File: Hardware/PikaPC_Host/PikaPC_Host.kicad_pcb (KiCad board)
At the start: 4 copper layers, 101.6 x 101.6 mm, 225 parts, among them J1 DE9_Pins_MountingHoles, J2 DIN41612_03x32_C_Split, J3 Conn_01x03, SW1 SW_Push, U1 PPC403GA, U10 74ALVC164245, U11 74ALVC164245, U12 74ALVC164245, U2 ATF1508AS, U3 MCP120-315GI/TO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

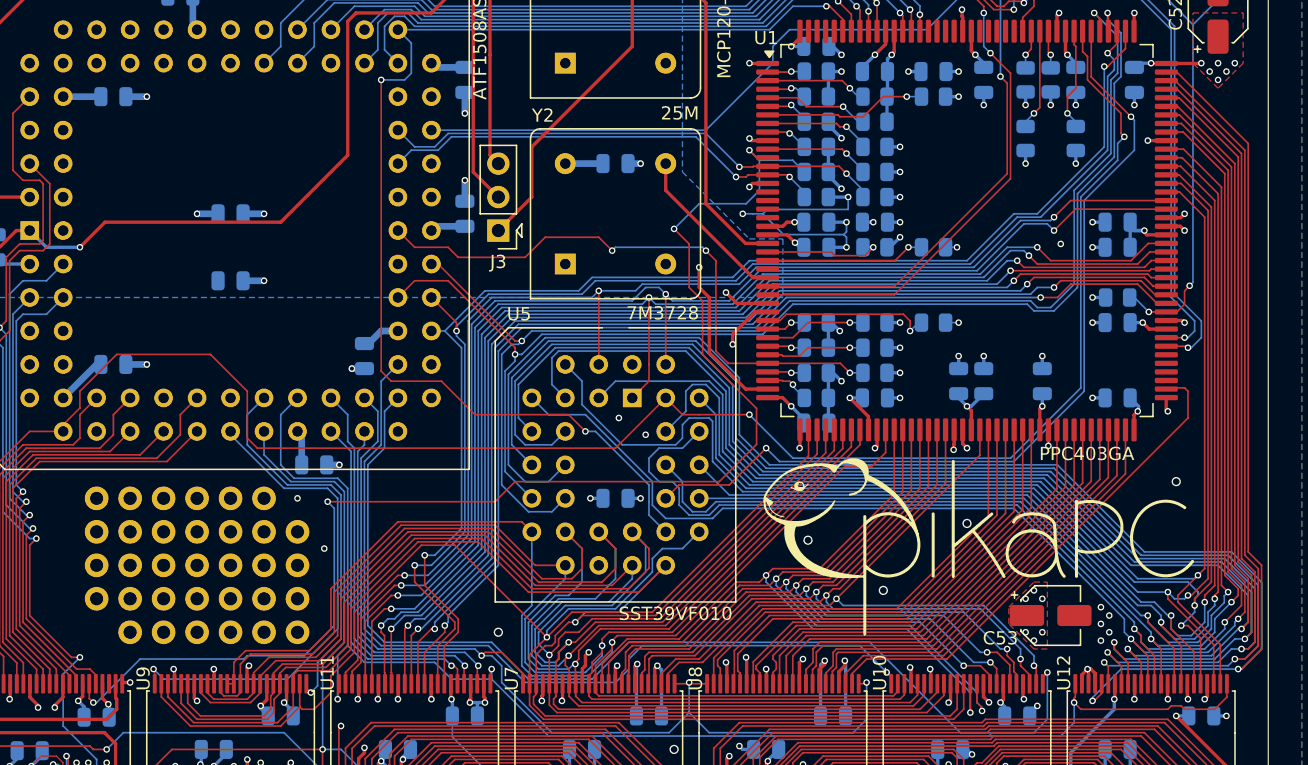
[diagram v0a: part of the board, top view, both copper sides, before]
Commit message: fix low two expansion bus address bits
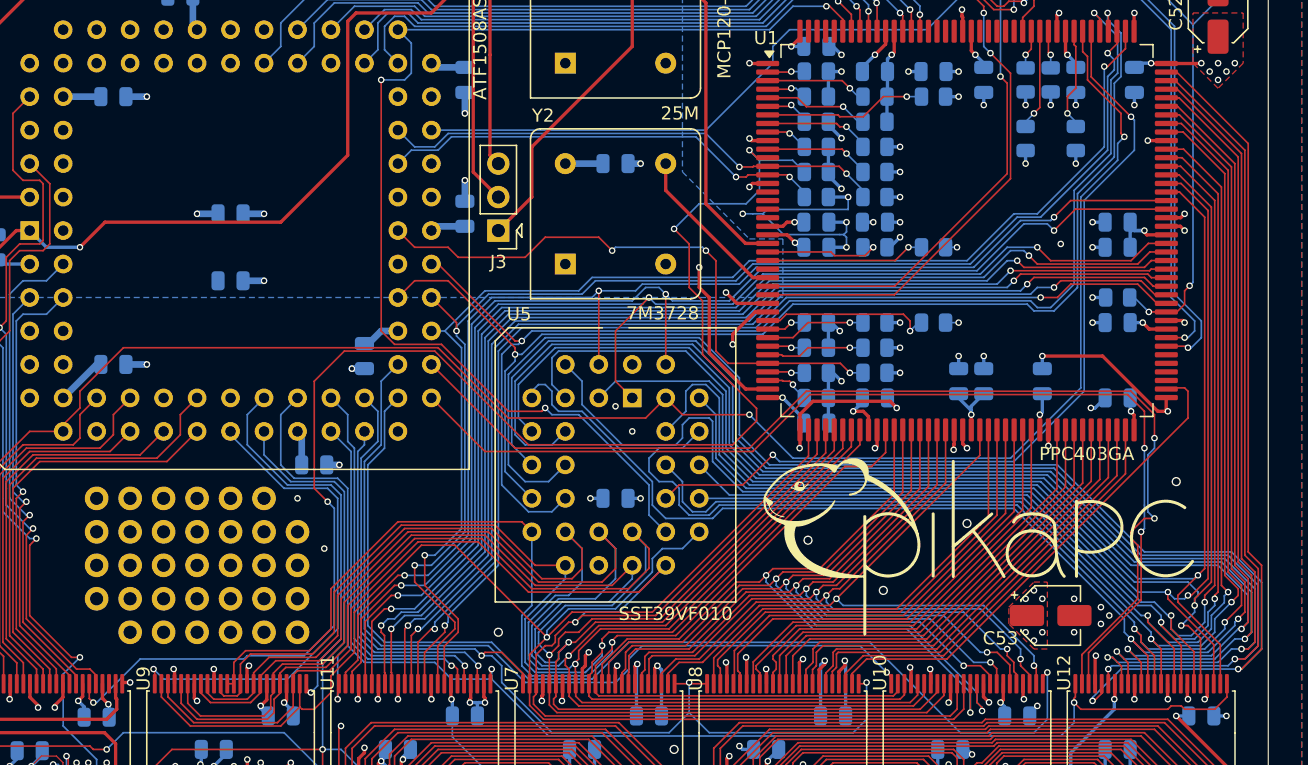
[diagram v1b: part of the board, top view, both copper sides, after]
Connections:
- U12 pad 46: GND -> /Main Bus/XA30
- U12 pad 47: GND -> /Main Bus/XA31
- U2 pad 33: unconnected-(U2A-IO64-Pad33) -> /Main Bus/XA30
- U2 pad 35: unconnected-(U2A-IO59-Pad35) -> /Main Bus/XA31
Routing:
- net /Main Bus/XA31: track 0.00 -> 84.0 mm, vias 0 -> 2
- net /Main Bus/XA30: track 0.00 -> 80.5 mm, vias 0 -> 2
- net GND: track 229.4 -> 248.5 mm
- net /CPU Bus/~{BusError}: track 101.6 -> 113.2 mm
- net /R/~{W}: track 144.1 -> 140.5 mm
- net /Main Bus/A24: track 110.5 -> 112.2 mm
- net /CPU Bus/~{CS0}: track 92.1 -> 90.5 mm
- net /Main Bus/A26: track 134.2 -> 132.6 mm
- net /Main Bus/A13: track 96.3 -> 97.4 mm
- net /Main Bus/A28: track 142.3 -> 141.4 mm

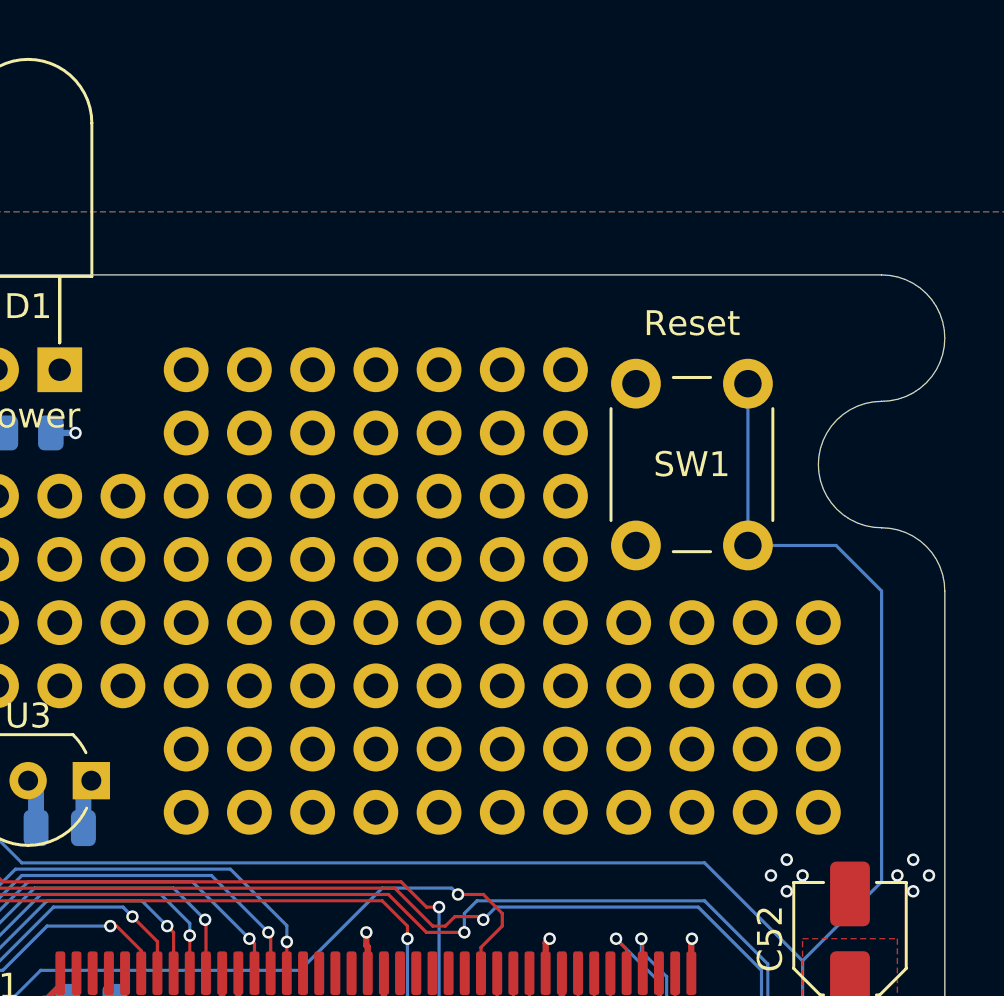
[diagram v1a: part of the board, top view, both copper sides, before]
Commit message: don't double-buffer bus clock, add missing bus control signal pull-ups
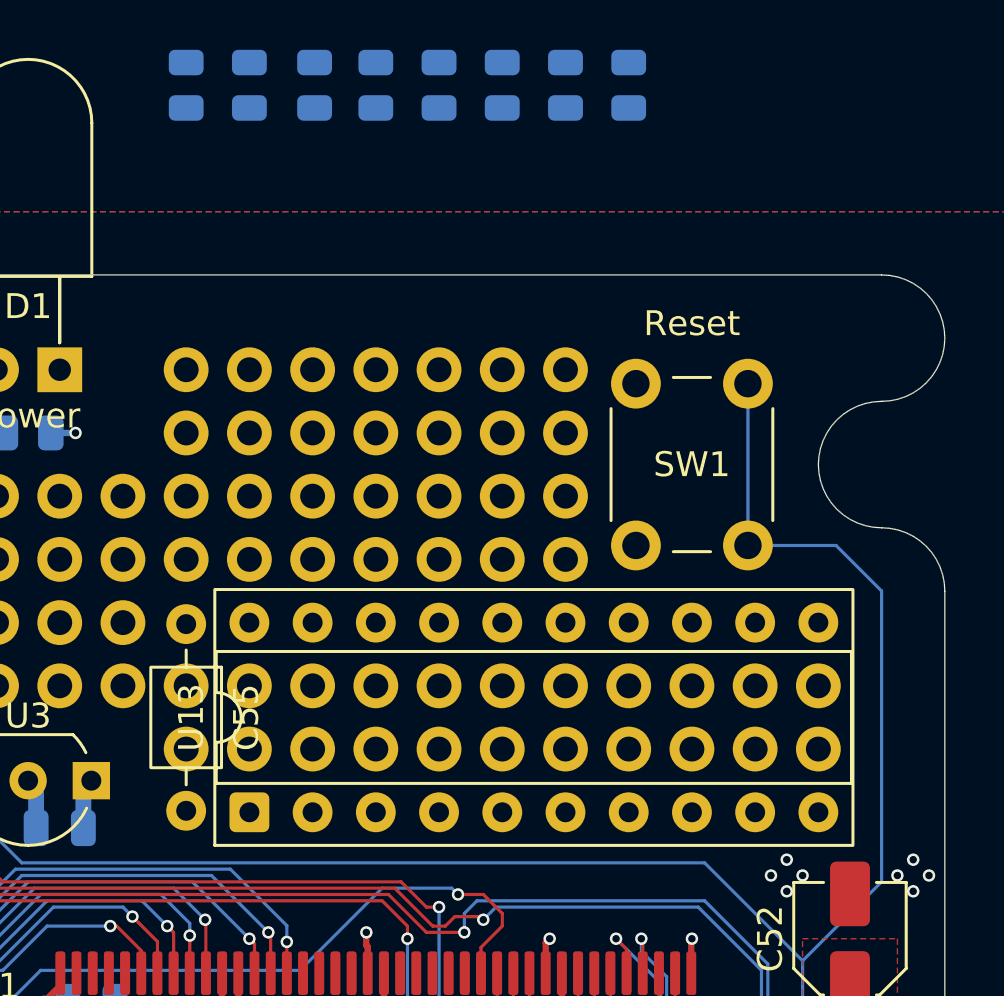
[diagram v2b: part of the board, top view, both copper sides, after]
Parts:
- removed the REF** at (149.9, 64.8)
- removed the REF** at (165.1, 64.8)
- removed the REF** at (167.6, 72.4)
- removed the REF** at (149.9, 72.4)
- removed the REF** at (152.4, 72.4)
- removed the REF** at (157.5, 72.4)
- removed the REF** at (154.9, 64.8)
- removed the REF** at (157.5, 64.8)
- removed the REF** at (172.7, 64.8)
- removed the REF** at (172.7, 72.4)
- removed the REF** at (152.4, 64.8)
- removed the REF** at (160.0, 72.4)
- removed the REF** at (162.6, 72.4)
- removed the REF** at (165.1, 72.4)
- removed the REF** at (147.3, 64.8)
- removed the REF** at (160.0, 64.8)
- removed the REF** at (162.6, 64.8)
- removed the REF** at (170.2, 64.8)
- removed the REF** at (170.2, 72.4)
- removed the REF** at (147.3, 72.4)
- removed the REF** at (154.9, 72.4)
- removed the REF** at (167.6, 64.8)
- added C55: 100nF, Capacitor_THT:C_Axial_L3.8mm_D2.6mm_P7.50mm_Horizontal, F.Cu at (147.3, 64.8)
- added R29: 4k7, Resistor_SMD:R_0805_2012Metric, B.Cu at (165.1, 43.2)
- added R30: 4k7, Resistor_SMD:R_0805_2012Metric, B.Cu at (162.6, 43.2)
- added R31: 4k7, Resistor_SMD:R_0805_2012Metric, B.Cu at (160.0, 43.2)
- added R32: 4k7, Resistor_SMD:R_0805_2012Metric, B.Cu at (157.5, 43.2)
- added R33: 4k7, Resistor_SMD:R_0805_2012Metric, B.Cu at (149.9, 43.2)
- added R34: 4k7, Resistor_SMD:R_0805_2012Metric, B.Cu at (154.9, 43.2)
- added R35: 4k7, Resistor_SMD:R_0805_2012Metric, B.Cu at (152.5, 43.2)
- added R36: 4k7, Resistor_SMD:R_0805_2012Metric, B.Cu at (147.3, 43.2)
- added U13: 74AHCT244, Package_DIP:DIP-20_W7.62mm_Socket, F.Cu at (149.9, 72.4)
